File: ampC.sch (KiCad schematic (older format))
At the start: 13 parts, among them U19 Mux, U6 MCP6004, U8 screw_term, U9 screw_term

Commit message: switched to sensor sheet for one sensor divider
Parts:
- removed R19, R20, R21: 330, Resistor_THT:R_Axial_DIN0204_L3.6mm_D1.6mm_P5.08mm_Horizontal, symbol Device:R
- removed U8, U9: screw_term, Connector_PinHeader_1.27mm:PinHeader_1x02_P1.27mm_Vertical, symbol PNG_PCB_Parts:screw_term
- renumbered R22 to R31, R23 to R32, R24 to R33, R25 to R34, R26 to R35, R27 to R36, U6 to U4, U19 to U8

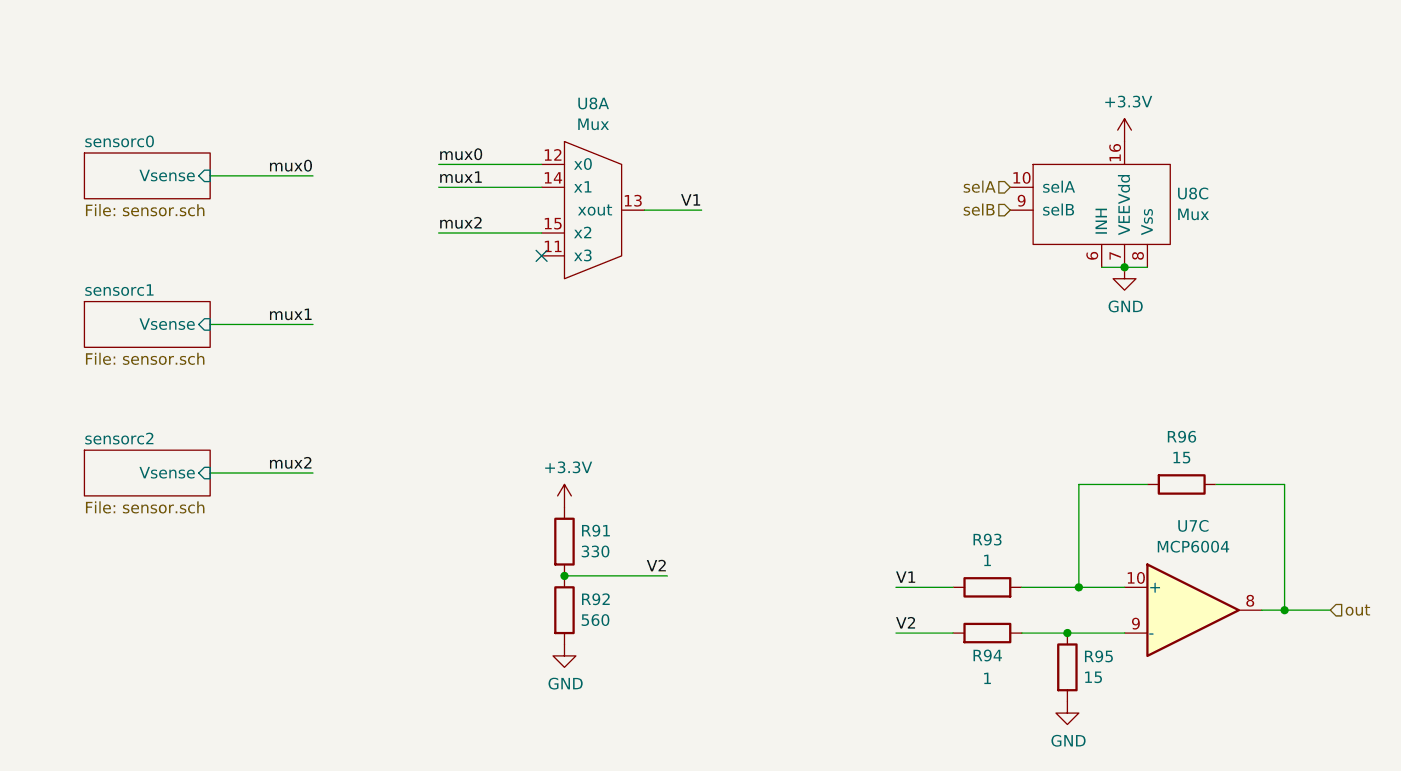
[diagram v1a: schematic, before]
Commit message: revised sensor connector
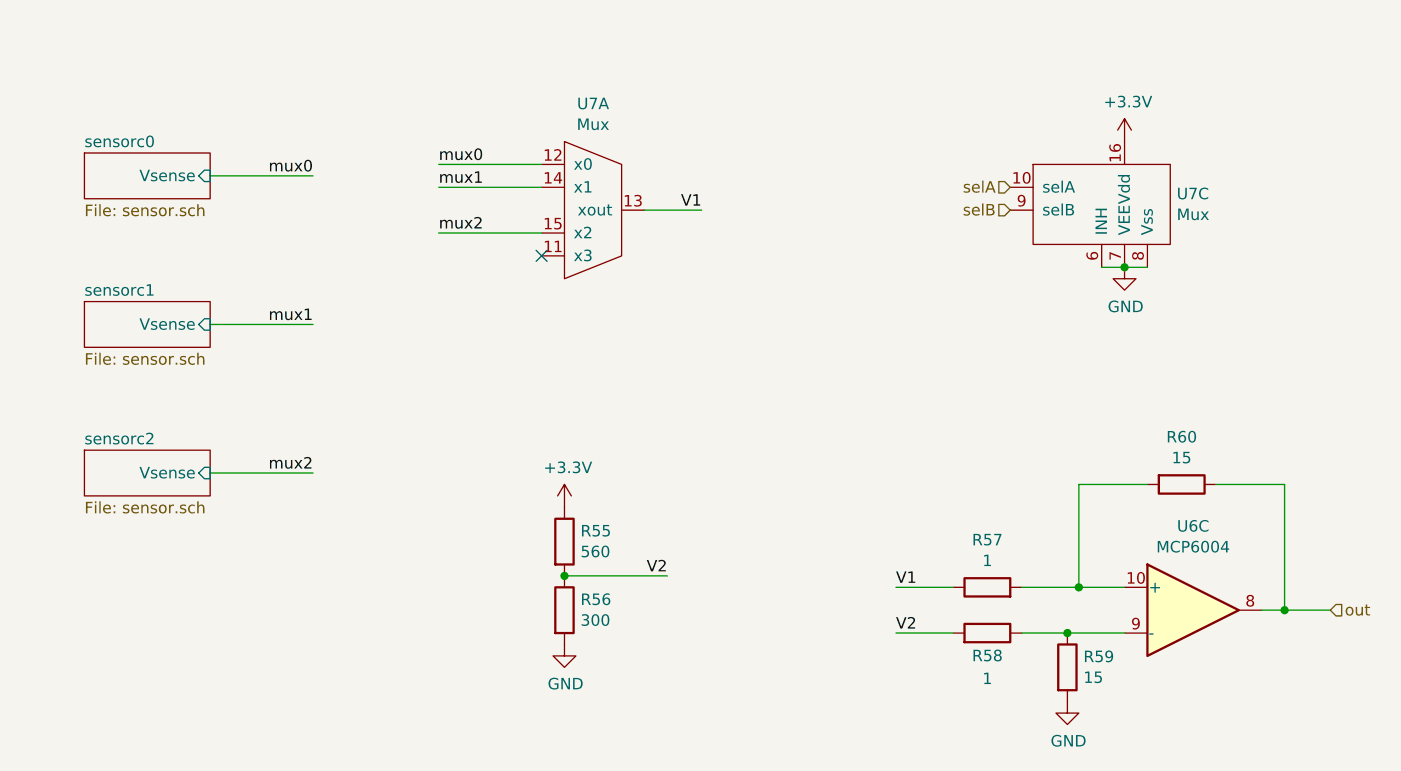
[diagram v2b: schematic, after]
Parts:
- R19: renamed from R31; value 330 -> 560
- R20: renamed from R32; value 560 -> 300
- renumbered R33 to R21, R34 to R22, R35 to R23, R36 to R24, U4 to U3, U8 to U7
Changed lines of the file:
@@
 $Descr A4 11693 8268
 encoding utf-8
-Sheet 10 41
+Sheet 26 41
 Title ""
 Date ""
@@
 AR Path="/6017DA21/60198F28" Ref="R?"  Part="1"
 AR Path="/601927EB/60198F28" Ref="R?"  Part="1"
-AR Path="/6019C043/60198F28" Ref="R35"  Part="1"
-AR Path="/601B4C16/60198F28" Ref="R95"  Part="1"
-F 0 "R95" H 5520 4096 50  0000 L CNN
+AR Path="/6019C043/60198F28" Ref="R23"  Part="1"
+AR Path="/601B4C16/60198F28" Ref="R59"  Part="1"
+F 0 "R59" H 5520 4096 50  0000 L CNN
 F 1 "15" H 5520 4005 50  0000 L CNN
 F 2 "Resistor_THT:R_Axial_DIN0204_L3.6mm_D1.6mm_P5.08mm_Horizontal" V 5380 4050 50  0001 C CNN
@@
 AR Path="/6017DA21/6019D567" Ref="R?"  Part="1"
 AR Path="/601927EB/6019D567" Ref="R?"  Part="1"
-AR Path="/6019C043/6019D567" Ref="R36"  Part="1"
-AR Path="/601B4C16/6019D567" Ref="R96"  Part="1"
-F 0 "R96" V 5743 3250 50  0000 C CNN
+AR Path="/6019C043/6019D567" Ref="R24"  Part="1"
+AR Path="/601B4C16/6019D567" Ref="R60"  Part="1"
+F 0 "R60" V 5743 3250 50  0000 C CNN
 F 1 "15" V 5834 3250 50  0000 C CNN
 F 2 "Resistor_THT:R_Axial_DIN0204_L3.6mm_D1.6mm_P5.08mm_Horizontal" V 5880 3250 50  0001 C CNN
@@
 AR Path="/6017DA21/6019D55D" Ref="R?"  Part="1"
 AR Path="/601927EB/6019D55D" Ref="R?"  Part="1"
-AR Path="/6019C043/6019D55D" Ref="R33"  Part="1"
-AR Path="/601B4C16/6019D55D" Ref="R93"  Part="1"
-F 0 "R93" V 5307 3700 50  0000 C CNN
+AR Path="/6019C043/6019D55D" Ref="R21"  Part="1"
+AR Path="/601B4C16/6019D55D" Ref="R57"  Part="1"
+F 0 "R57" V 5307 3700 50  0000 C CNN
 F 1 "1" V 5216 3700 50  0000 C CNN
 F 2 "Resistor_THT:R_Axial_DIN0204_L3.6mm_D1.6mm_P5.08mm_Horizontal" V 5030 3700 50  0001 C CNN
@@
 AR Path="/6017DA21/60198F34" Ref="R?"  Part="1"
 AR Path="/601927EB/60198F34" Ref="R?"  Part="1"
-AR Path="/6019C043/60198F34" Ref="R34"  Part="1"
-AR Path="/601B4C16/60198F34" Ref="R94"  Part="1"
-F 0 "R94" V 5000 3900 50  0000 C CNN
+AR Path="/6019C043/60198F34" Ref="R22"  Part="1"
+AR Path="/601B4C16/60198F34" Ref="R58"  Part="1"
+F 0 "R58" V 5000 3900 50  0000 C CNN
 F 1 "1" V 4900 3900 50  0000 C CNN
 F 2 "Resistor_THT:R_Axial_DIN0204_L3.6mm_D1.6mm_P5.08mm_Horizontal" V 5030 3900 50  0001 C CNN
@@
 AR Path="/6017DA21/6017E433" Ref="R?"  Part="1"
 AR Path="/601927EB/6017E433" Ref="R?"  Part="1"
-AR Path="/6019C043/6017E433" Ref="R31"  Part="1"
-AR Path="/601B4C16/6017E433" Ref="R91"  Part="1"
-F 0 "R91" H 3320 3546 50  0000 L CNN
-F 1 "330" H 3320 3455 50  0000 L CNN
+AR Path="/6019C043/6017E433" Ref="R19"  Part="1"
+AR Path="/601B4C16/6017E433" Ref="R55"  Part="1"
+F 0 "R55" H 3320 3546 50  0000 L CNN
+F 1 "560" H 3320 3455 50  0000 L CNN
 F 2 "Resistor_THT:R_Axial_DIN0204_L3.6mm_D1.6mm_P5.08mm_Horizontal" V 3180 3500 50  0001 C CNN
 F 3 "~" H 3250 3500 50  0001 C CNN
@@
 AR Path="/6017DA21/6017E434" Ref="R?"  Part="1"
 AR Path="/601927EB/6017E434" Ref="R?"  Part="1"
-AR Path="/6019C043/6017E434" Ref="R32"  Part="1"
-AR Path="/601B4C16/6017E434" Ref="R92"  Part="1"
-F 0 "R92" H 3320 3846 50  0000 L CNN
-F 1 "560" H 3320 3755 50  0000 L CNN
+AR Path="/6019C043/6017E434" Ref="R20"  Part="1"
+AR Path="/601B4C16/6017E434" Ref="R56"  Part="1"
+F 0 "R56" H 3320 3846 50  0000 L CNN
+F 1 "300" H 3320 3755 50  0000 L CNN
 F 2 "Resistor_THT:R_Axial_DIN0204_L3.6mm_D1.6mm_P5.08mm_Horizontal" V 3180 3800 50  0001 C CNN
 F 3 "~" H 3250 3800 50  0001 C CNN
@@
 AR Path="/6017DA21/6017E435" Ref="#PWR?"  Part="1"
 AR Path="/601927EB/6017E435" Ref="#PWR?"  Part="1"
-AR Path="/6019C043/6017E435" Ref="#PWR054"  Part="1"
-AR Path="/601B4C16/6017E435" Ref="#PWR0144"  Part="1"
-F 0 "#PWR0144" H 3250 3200 50  0001 C CNN
+AR Path="/6019C043/6017E435" Ref="#PWR030"  Part="1"
+AR Path="/601B4C16/6017E435" Ref="#PWR072"  Part="1"
+F 0 "#PWR072" H 3250 3200 50  0001 C CNN
 F 1 "+3.3V" H 3265 3523 50  0000 C CNN
 F 2 "" H 3250 3350 50  0001 C CNN
@@
 AR Path="/6017DA21/6019D569" Ref="#PWR?"  Part="1"
 AR Path="/601927EB/6019D569" Ref="#PWR?"  Part="1"
-AR Path="/6019C043/6019D569" Ref="#PWR055"  Part="1"
-AR Path="/601B4C16/6019D569" Ref="#PWR0145"  Part="1"
-F 0 "#PWR0145" H 3250 3700 50  0001 C CNN
+AR Path="/6019C043/6019D569" Ref="#PWR031"  Part="1"
+AR Path="/601B4C16/6019D569" Ref="#PWR073"  Part="1"
+F 0 "#PWR073" H 3250 3700 50  0001 C CNN
 F 1 "GND" H 3255 3777 50  0000 C CNN
 F 2 "" H 3250 3950 50  0001 C CNN
@@
 AR Path="/6017DA21/6019D555" Ref="#PWR?"  Part="1"
 AR Path="/601927EB/6019D555" Ref="#PWR?"  Part="1"
-AR Path="/6019C043/6019D555" Ref="#PWR056"  Part="1"
-AR Path="/601B4C16/6019D555" Ref="#PWR0146"  Part="1"
-F 0 "#PWR0146" H 5450 3950 50  0001 C CNN
+AR Path="/6019C043/6019D555" Ref="#PWR032"  Part="1"
+AR Path="/601B4C16/6019D555" Ref="#PWR074"  Part="1"
+F 0 "#PWR074" H 5450 3950 50  0001 C CNN
 F 1 "GND" H 5455 4027 50  0000 C CNN
 F 2 "" H 5450 4200 50  0001 C CNN
@@
 AR Path="/6017DA21/6019D563" Ref="#PWR?"  Part="1"
 AR Path="/601927EB/6019D563" Ref="#PWR?"  Part="1"
-AR Path="/6019C043/6019D563" Ref="#PWR058"  Part="1"
-AR Path="/601B4C16/6019D563" Ref="#PWR0148"  Part="1"
-F 0 "#PWR0148" H 5700 2050 50  0001 C CNN
+AR Path="/6019C043/6019D563" Ref="#PWR034"  Part="1"
+AR Path="/601B4C16/6019D563" Ref="#PWR076"  Part="1"
+F 0 "#PWR076" H 5700 2050 50  0001 C CNN
 F 1 "GND" H 5705 2127 50  0000 C CNN
 F 2 "" H 5700 2300 50  0001 C CNN
@@
 AR Path="/6017CC5E/6019D564" Ref="#PWR?"  Part="1"
 AR Path="/601927EB/6019D564" Ref="#PWR?"  Part="1"
-AR Path="/6019C043/6019D564" Ref="#PWR057"  Part="1"
-AR Path="/601B4C16/6019D564" Ref="#PWR0147"  Part="1"
-F 0 "#PWR0147" H 5700 1600 50  0001 C CNN
+AR Path="/6019C043/6019D564" Ref="#PWR033"  Part="1"
+AR Path="/601B4C16/6019D564" Ref="#PWR075"  Part="1"
+F 0 "#PWR075" H 5700 1600 50  0001 C CNN
 F 1 "+3.3V" H 5715 1923 50  0000 C CNN
 F 2 "" H 5700 1750 50  0001 C CNN
@@
 selB
 $Comp
-L PNG_PCB_Parts:Mux U8
+L PNG_PCB_Parts:Mux U7
 U 1 1 601763C1
 P 3350 2050
-AR Path="/601B4C16/601763C1" Ref="U8"  Part="1"
-AR Path="/6019C043/601763C1" Ref="U5"  Part="1"
-F 0 "U8" H 3375 2515 50  0000 C CNN
+AR Path="/601B4C16/601763C1" Ref="U7"  Part="1"
+AR Path="/6019C043/601763C1" Ref="U4"  Part="1"
+F 0 "U7" H 3375 2515 50  0000 C CNN
 F 1 "Mux" H 3375 2424 50  0000 C CNN
 F 2 "Package_DIP:DIP-16_W7.62mm" H 3350 2050 50  0001 C CNN
@@
 $EndComp
 $Comp
-L PNG_PCB_Parts:Mux U8
+L PNG_PCB_Parts:Mux U7
 U 3 1 60176BAF
 P 5700 2100
-AR Path="/601B4C16/60176BAF" Ref="U8"  Part="3"
-AR Path="/6019C043/60176BAF" Ref="U5"  Part="3"
-F 0 "U8" H 5928 2221 50  0000 L CNN
+AR Path="/601B4C16/60176BAF" Ref="U7"  Part="3"
+AR Path="/6019C043/60176BAF" Ref="U4"  Part="3"
+F 0 "U7" H 5928 2221 50  0000 L CNN
 F 1 "Mux" H 5928 2130 50  0000 L CNN
 F 2 "Package_DIP:DIP-16_W7.62mm" H 5700 2100 50  0001 C CNN
@@
 $EndComp
 $Comp
-L Amplifier_Operational:MCP6004 U4
+L Amplifier_Operational:MCP6004 U3
 U 3 1 6018DE62
 P 6000 3800
-AR Path="/6019C043/6018DE62" Ref="U4"  Part="3"
-AR Path="/601B4C16/6018DE62" Ref="U7"  Part="3"
-F 0 "U7" H 6000 4167 50  0000 C CNN
+AR Path="/6019C043/6018DE62" Ref="U3"  Part="3"
+AR Path="/601B4C16/6018DE62" Ref="U6"  Part="3"
+F 0 "U6" H 6000 4167 50  0000 C CNN
 F 1 "MCP6004" H 6000 4076 50  0000 C CNN
 F 2 "Package_DIP:DIP-14_W7.62mm" H 5950 3900 50  0001 C CNN

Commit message: moved sensor r div to other side of mux
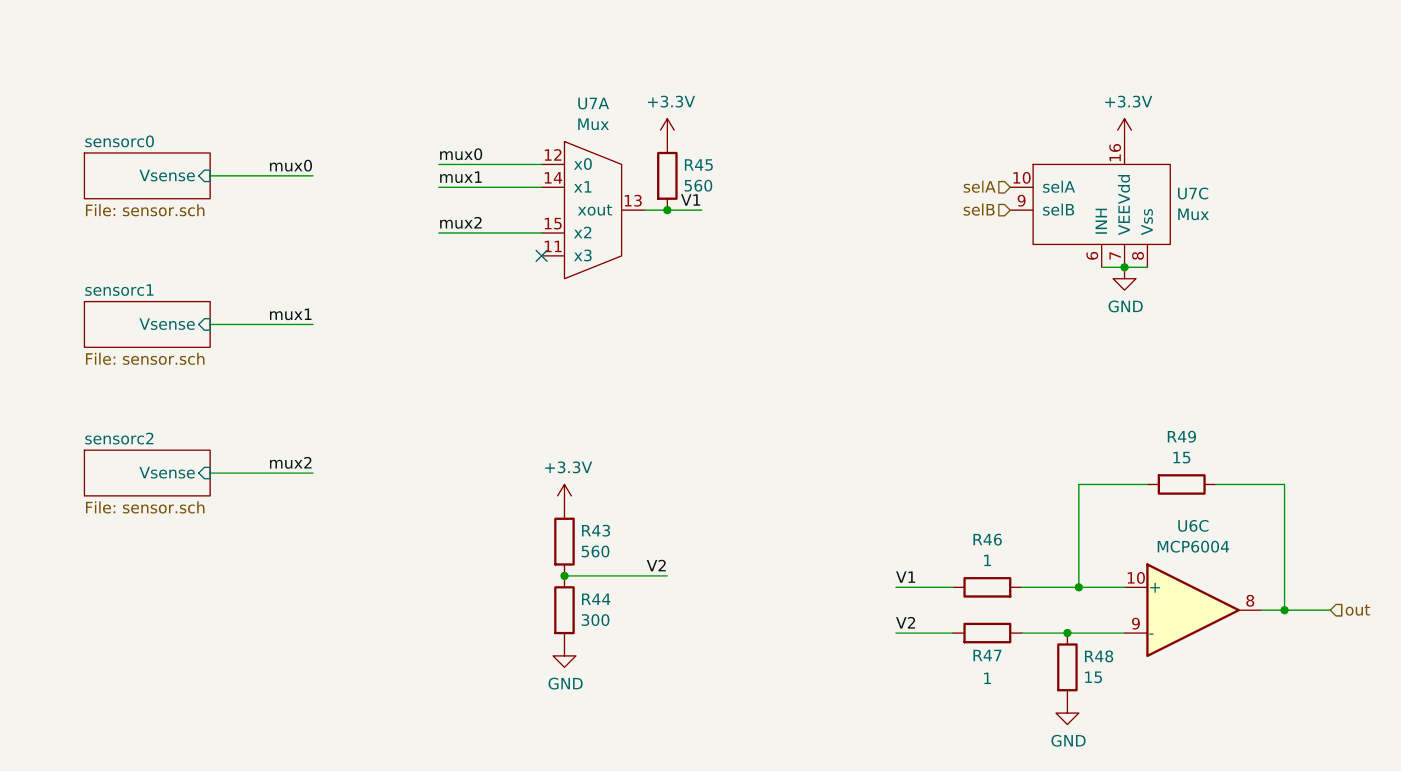
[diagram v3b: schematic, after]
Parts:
- added R17: 560, Resistor_THT:R_Axial_DIN0204_L3.6mm_D1.6mm_P5.08mm_Horizontal, symbol Device:R
- renumbered R19 to R15, R20 to R16, R21 to R18, R22 to R19, R23 to R20, R24 to R21
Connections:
- net +3V3: now also R17.1
- net V1: now also R17.2
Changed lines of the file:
@@
 $Descr A4 11693 8268
 encoding utf-8
-Sheet 26 41
+Sheet 10 41
 Title ""
 Date ""
@@
 AR Path="/6017DA21/60198F28" Ref="R?"  Part="1"
 AR Path="/601927EB/60198F28" Ref="R?"  Part="1"
-AR Path="/6019C043/60198F28" Ref="R23"  Part="1"
-AR Path="/601B4C16/60198F28" Ref="R59"  Part="1"
-F 0 "R59" H 5520 4096 50  0000 L CNN
+AR Path="/6019C043/60198F28" Ref="R20"  Part="1"
+AR Path="/601B4C16/60198F28" Ref="R48"  Part="1"
+F 0 "R48" H 5520 4096 50  0000 L CNN
 F 1 "15" H 5520 4005 50  0000 L CNN
 F 2 "Resistor_THT:R_Axial_DIN0204_L3.6mm_D1.6mm_P5.08mm_Horizontal" V 5380 4050 50  0001 C CNN
@@
 AR Path="/6017DA21/6019D567" Ref="R?"  Part="1"
 AR Path="/601927EB/6019D567" Ref="R?"  Part="1"
-AR Path="/6019C043/6019D567" Ref="R24"  Part="1"
-AR Path="/601B4C16/6019D567" Ref="R60"  Part="1"
-F 0 "R60" V 5743 3250 50  0000 C CNN
+AR Path="/6019C043/6019D567" Ref="R21"  Part="1"
+AR Path="/601B4C16/6019D567" Ref="R49"  Part="1"
+F 0 "R49" V 5743 3250 50  0000 C CNN
 F 1 "15" V 5834 3250 50  0000 C CNN
 F 2 "Resistor_THT:R_Axial_DIN0204_L3.6mm_D1.6mm_P5.08mm_Horizontal" V 5880 3250 50  0001 C CNN
@@
 AR Path="/6017DA21/6019D55D" Ref="R?"  Part="1"
 AR Path="/601927EB/6019D55D" Ref="R?"  Part="1"
-AR Path="/6019C043/6019D55D" Ref="R21"  Part="1"
-AR Path="/601B4C16/6019D55D" Ref="R57"  Part="1"
-F 0 "R57" V 5307 3700 50  0000 C CNN
+AR Path="/6019C043/6019D55D" Ref="R18"  Part="1"
+AR Path="/601B4C16/6019D55D" Ref="R46"  Part="1"
+F 0 "R46" V 5307 3700 50  0000 C CNN
 F 1 "1" V 5216 3700 50  0000 C CNN
 F 2 "Resistor_THT:R_Axial_DIN0204_L3.6mm_D1.6mm_P5.08mm_Horizontal" V 5030 3700 50  0001 C CNN
@@
 AR Path="/6017DA21/60198F34" Ref="R?"  Part="1"
 AR Path="/601927EB/60198F34" Ref="R?"  Part="1"
-AR Path="/6019C043/60198F34" Ref="R22"  Part="1"
-AR Path="/601B4C16/60198F34" Ref="R58"  Part="1"
-F 0 "R58" V 5000 3900 50  0000 C CNN
+AR Path="/6019C043/60198F34" Ref="R19"  Part="1"
+AR Path="/601B4C16/60198F34" Ref="R47"  Part="1"
+F 0 "R47" V 5000 3900 50  0000 C CNN
 F 1 "1" V 4900 3900 50  0000 C CNN
 F 2 "Resistor_THT:R_Axial_DIN0204_L3.6mm_D1.6mm_P5.08mm_Horizontal" V 5030 3900 50  0001 C CNN
@@
 	4950 3900 4700 3900
 Wire Wire Line
-	3600 2050 3850 2050
+	3600 2050 3700 2050
 Text Label 3850 2050 2    50   ~ 0
 V1
@@
 AR Path="/6017DA21/6017E433" Ref="R?"  Part="1"
 AR Path="/601927EB/6017E433" Ref="R?"  Part="1"
-AR Path="/6019C043/6017E433" Ref="R19"  Part="1"
-AR Path="/601B4C16/6017E433" Ref="R55"  Part="1"
-F 0 "R55" H 3320 3546 50  0000 L CNN
+AR Path="/6019C043/6017E433" Ref="R15"  Part="1"
+AR Path="/601B4C16/6017E433" Ref="R43"  Part="1"
+F 0 "R43" H 3320 3546 50  0000 L CNN
 F 1 "560" H 3320 3455 50  0000 L CNN
 F 2 "Resistor_THT:R_Axial_DIN0204_L3.6mm_D1.6mm_P5.08mm_Horizontal" V 3180 3500 50  0001 C CNN
@@
 AR Path="/6017DA21/6017E434" Ref="R?"  Part="1"
 AR Path="/601927EB/6017E434" Ref="R?"  Part="1"
-AR Path="/6019C043/6017E434" Ref="R20"  Part="1"
-AR Path="/601B4C16/6017E434" Ref="R56"  Part="1"
-F 0 "R56" H 3320 3846 50  0000 L CNN
+AR Path="/6019C043/6017E434" Ref="R16"  Part="1"
+AR Path="/601B4C16/6017E434" Ref="R44"  Part="1"
+F 0 "R44" H 3320 3846 50  0000 L CNN
 F 1 "300" H 3320 3755 50  0000 L CNN
 F 2 "Resistor_THT:R_Axial_DIN0204_L3.6mm_D1.6mm_P5.08mm_Horizontal" V 3180 3800 50  0001 C CNN
@@
 AR Path="/6017DA21/6017E435" Ref="#PWR?"  Part="1"
 AR Path="/601927EB/6017E435" Ref="#PWR?"  Part="1"
-AR Path="/6019C043/6017E435" Ref="#PWR030"  Part="1"
-AR Path="/601B4C16/6017E435" Ref="#PWR072"  Part="1"
-F 0 "#PWR072" H 3250 3200 50  0001 C CNN
+AR Path="/6019C043/6017E435" Ref="#PWR026"  Part="1"
+AR Path="/601B4C16/6017E435" Ref="#PWR060"  Part="1"
+F 0 "#PWR060" H 3250 3200 50  0001 C CNN
 F 1 "+3.3V" H 3265 3523 50  0000 C CNN
 F 2 "" H 3250 3350 50  0001 C CNN
@@
 AR Path="/6017DA21/6019D569" Ref="#PWR?"  Part="1"
 AR Path="/601927EB/6019D569" Ref="#PWR?"  Part="1"
-AR Path="/6019C043/6019D569" Ref="#PWR031"  Part="1"
-AR Path="/601B4C16/6019D569" Ref="#PWR073"  Part="1"
-F 0 "#PWR073" H 3250 3700 50  0001 C CNN
+AR Path="/6019C043/6019D569" Ref="#PWR027"  Part="1"
+AR Path="/601B4C16/6019D569" Ref="#PWR061"  Part="1"
+F 0 "#PWR061" H 3250 3700 50  0001 C CNN
 F 1 "GND" H 3255 3777 50  0000 C CNN
 F 2 "" H 3250 3950 50  0001 C CNN
@@
 AR Path="/6017DA21/6019D555" Ref="#PWR?"  Part="1"
 AR Path="/601927EB/6019D555" Ref="#PWR?"  Part="1"
-AR Path="/6019C043/6019D555" Ref="#PWR032"  Part="1"
-AR Path="/601B4C16/6019D555" Ref="#PWR074"  Part="1"
-F 0 "#PWR074" H 5450 3950 50  0001 C CNN
+AR Path="/6019C043/6019D555" Ref="#PWR029"  Part="1"
+AR Path="/601B4C16/6019D555" Ref="#PWR063"  Part="1"
+F 0 "#PWR063" H 5450 3950 50  0001 C CNN
 F 1 "GND" H 5455 4027 50  0000 C CNN
 F 2 "" H 5450 4200 50  0001 C CNN
@@
 AR Path="/6017DA21/6019D563" Ref="#PWR?"  Part="1"
 AR Path="/601927EB/6019D563" Ref="#PWR?"  Part="1"
-AR Path="/6019C043/6019D563" Ref="#PWR034"  Part="1"
-AR Path="/601B4C16/6019D563" Ref="#PWR076"  Part="1"
-F 0 "#PWR076" H 5700 2050 50  0001 C CNN
+AR Path="/6019C043/6019D563" Ref="#PWR031"  Part="1"
+AR Path="/601B4C16/6019D563" Ref="#PWR065"  Part="1"
+F 0 "#PWR065" H 5700 2050 50  0001 C CNN
 F 1 "GND" H 5705 2127 50  0000 C CNN
 F 2 "" H 5700 2300 50  0001 C CNN
@@
 AR Path="/6017CC5E/6019D564" Ref="#PWR?"  Part="1"
 AR Path="/601927EB/6019D564" Ref="#PWR?"  Part="1"
-AR Path="/6019C043/6019D564" Ref="#PWR033"  Part="1"
-AR Path="/601B4C16/6019D564" Ref="#PWR075"  Part="1"
-F 0 "#PWR075" H 5700 1600 50  0001 C CNN
+AR Path="/6019C043/6019D564" Ref="#PWR030"  Part="1"
+AR Path="/601B4C16/6019D564" Ref="#PWR064"  Part="1"
+F 0 "#PWR064" H 5700 1600 50  0001 C CNN
 F 1 "+3.3V" H 5715 1923 50  0000 C CNN
 F 2 "" H 5700 1750 50  0001 C CNN
@@
 F2 "Vsense" I R 1700 3200 50
 $EndSheet
+$Comp
+L Device:R R?
+U 1 1 60205F03
+P 3700 1900
+AR Path="/60132BC3/6013AE22/60205F03" Ref="R?"  Part="1"
+AR Path="/6017CC5E/60205F03" Ref="R?"  Part="1"
+AR Path="/6017DA21/60205F03" Ref="R?"  Part="1"
+AR Path="/601927EB/60205F03" Ref="R?"  Part="1"
+AR Path="/6019C043/60205F03" Ref="R17"  Part="1"
+AR Path="/601B4C16/60205F03" Ref="R45"  Part="1"
+F 0 "R45" H 3770 1946 50  0000 L CNN
+F 1 "560" H 3770 1855 50  0000 L CNN
+F 2 "Resistor_THT:R_Axial_DIN0204_L3.6mm_D1.6mm_P5.08mm_Horizontal" V 3630 1900 50  0001 C CNN
+F 3 "~" H 3700 1900 50  0001 C CNN
+	1    3700 1900
+	1    0    0    -1
+$EndComp
+Connection ~ 3700 2050
+Wire Wire Line
+	3700 2050 3850 2050
+$Comp
+L power:+3.3V #PWR?
+U 1 1 60206022
+P 3700 1750
+AR Path="/60132BC3/6013AE22/60206022" Ref="#PWR?"  Part="1"
+AR Path="/6017CC5E/60206022" Ref="#PWR?"  Part="1"
+AR Path="/6017DA21/60206022" Ref="#PWR?"  Part="1"
+AR Path="/601927EB/60206022" Ref="#PWR?"  Part="1"
+AR Path="/6019C043/60206022" Ref="#PWR028"  Part="1"
+AR Path="/601B4C16/60206022" Ref="#PWR062"  Part="1"
+F 0 "#PWR062" H 3700 1600 50  0001 C CNN
+F 1 "+3.3V" H 3715 1923 50  0000 C CNN
+F 2 "" H 3700 1750 50  0001 C CNN
+F 3 "" H 3700 1750 50  0001 C CNN
+	1    3700 1750
+	1    0    0    -1
+$EndComp
 $EndSCHEMATC
